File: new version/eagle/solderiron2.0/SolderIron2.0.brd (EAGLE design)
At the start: 36 x 47 mm, 36 parts, among them J1 DCJ0202, X1 22-23-2021, X2 PG203J

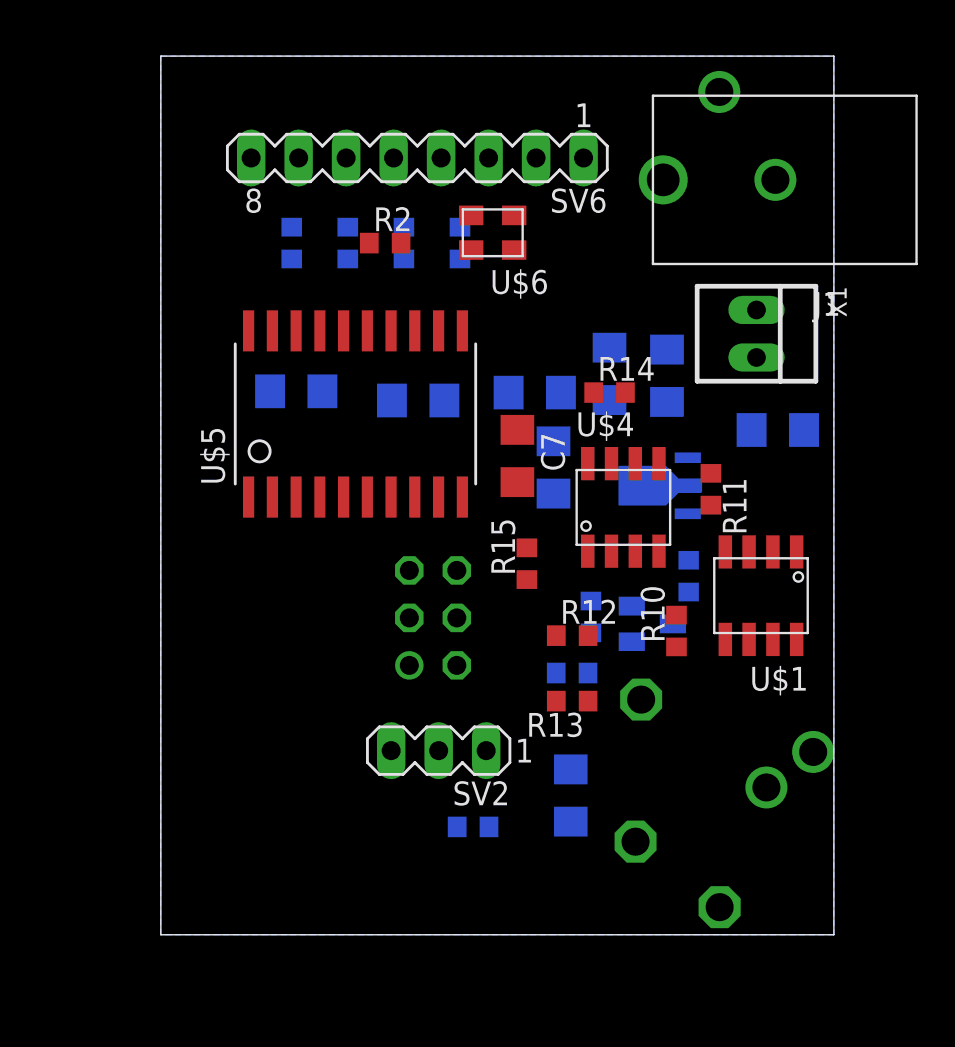
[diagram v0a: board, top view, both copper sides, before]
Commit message: routed new board
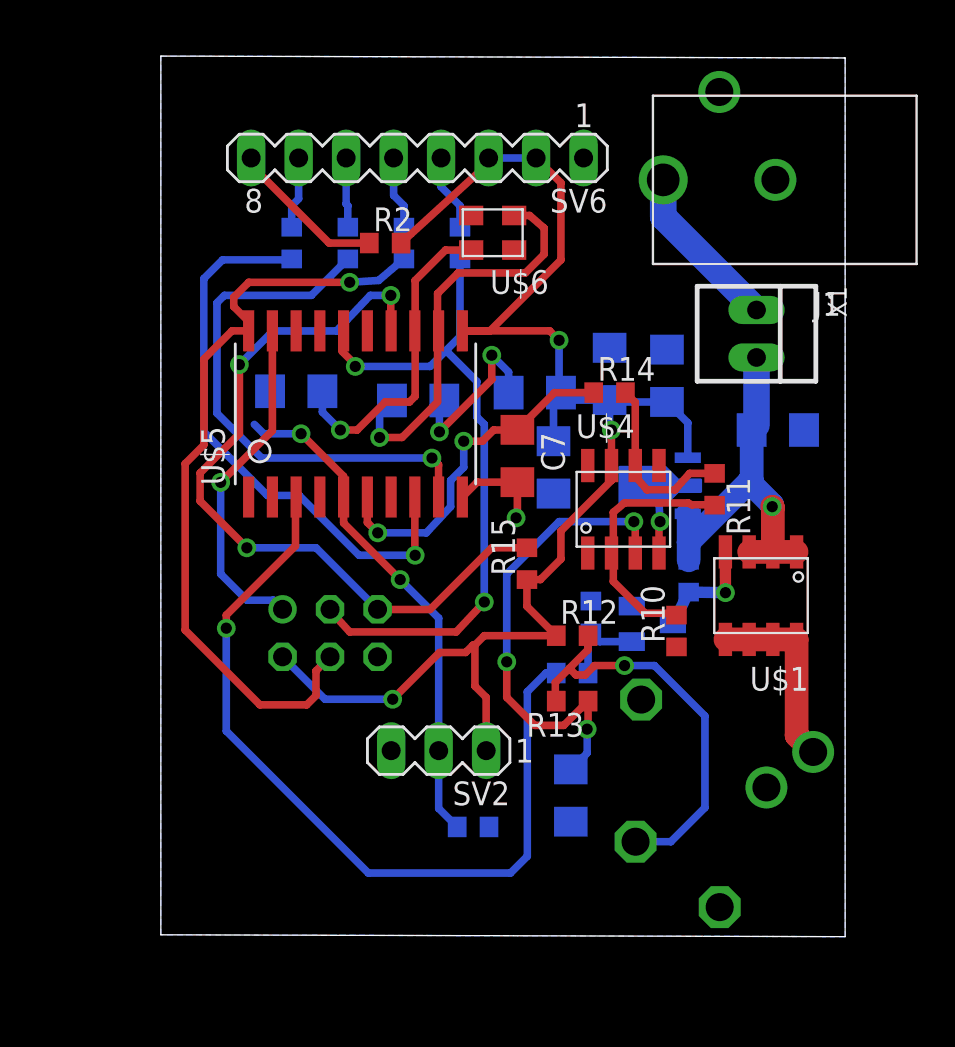
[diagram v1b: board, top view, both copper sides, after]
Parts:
- moved SV4 5.57 mm to (25.1, 34.1), turned to 180 degrees
- moved R11 0.20 mm to (45.6, 41.8)
- moved U$4 0.10 mm to (40.7, 40.8)
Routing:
- net +5V: track 0.00 -> 80.8 mm, vias 0 -> 3
- net PWM: track 0.00 -> 44.4 mm, vias 0 -> 1
- net MOSI: track 0.00 -> 41.2 mm, vias 0 -> 1
- net N$19: track 0.00 -> 41.0 mm, vias 0 -> 3
- net SCK: track 0.00 -> 36.4 mm, vias 0 -> 2
- net CS: track 0.00 -> 30.5 mm, vias 0 -> 1
- net DC: track 0.00 -> 28.6 mm, vias 0 -> 1
- net POT: track 0.00 -> 27.2 mm, vias 0 -> 2
- net N$13: track 0.00 -> 25.8 mm, vias 0 -> 3
- net SEN: track 0.00 -> 22.3 mm, vias 0 -> 1
- net N$14: track 0.00 -> 21.8 mm, vias 0 -> 1
- net V12: track 0.00 -> 20.7 mm, vias 0 -> 1
- net ADC: track 0.00 -> 18.6 mm, vias 0 -> 2
- net GND: track 0.00 -> 18.3 mm, vias 0 -> 4
- net N$15: track 0.00 -> 18.2 mm, vias 0 -> 1
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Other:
- board size 36 x 47 mm -> 36.6 x 47.1 mm

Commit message: added title to PCB
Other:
- board size 36.6 x 47.1 mm -> 37.6 x 51.1 mm
- board text added: "By: BLKBNY"
- board text added: "Solder Station V2.0"
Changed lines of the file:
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@@
 <setting verticaltext="up"/>
 </settings>
-<grid distance="0.1" unitdist="mm" unit="mm" style="lines" multiple="1" display="yes" altdistance="0.025" altunitdist="inch" altunit="inch"/>
+<grid distance="1" unitdist="mm" unit="mm" style="lines" multiple="1" display="yes" altdistance="0.025" altunitdist="inch" altunit="inch"/>
 <layers>
 <layer number="1" name="Top" color="4" fill="1" visible="yes" active="yes"/>
@@
 <board>
 <plain>
-<wire x1="16" y1="18" x2="52.6" y2="17.9" width="0" layer="20"/>
-<wire x1="52.6" y1="17.9" x2="52.6" y2="64.9" width="0" layer="20"/>
-<wire x1="52.6" y1="64.9" x2="16" y2="65" width="0" layer="20"/>
-<wire x1="16" y1="65" x2="16" y2="18" width="0" layer="20"/>
+<wire x1="16" y1="15" x2="53.6" y2="14.9" width="0" layer="20"/>
+<wire x1="53.6" y1="14.9" x2="53.6" y2="65.9" width="0" layer="20"/>
+<wire x1="53.6" y1="65.9" x2="16" y2="66" width="0" layer="20"/>
+<wire x1="16" y1="66" x2="16" y2="15" width="0" layer="20"/>
+<text x="39" y="22" size="1.778" layer="1" rot="R180">Solder Station V2.0 </text>
+<text x="31" y="19" size="1.778" layer="1" rot="R180">By: BLKBNY</text>
 </plain>
 <attributes>
@@
 <contactref element="C9" pad="2"/>
 <contactref element="C8" pad="2"/>
-<polygon width="0.4064" layer="16">
-<vertex x="16" y="65"/>
-<vertex x="52.6" y="64.9"/>
-<vertex x="52.6" y="17.9"/>
-<vertex x="16" y="18"/>
-</polygon>
 <wire x1="35.07" y1="42.21" x2="32.92" y2="42.21" width="0.4064" layer="1"/>
 <wire x1="32.92" y1="42.21" x2="32.125" y2="41.415" width="0.4064" layer="1"/>
@@
 <wire x1="35.07" y1="42.21" x2="35.07" y2="40.37" width="0.4064" layer="1"/>
 <wire x1="35.07" y1="40.37" x2="35" y2="40.3" width="0.4064" layer="1"/>
+<polygon width="0.4064" layer="16">
+<vertex x="17" y="66"/>
+<vertex x="54" y="66" curve="-90"/>
+<vertex x="55" y="65"/>
+<vertex x="55" y="15" curve="-90"/>
+<vertex x="54" y="14"/>
+<vertex x="16" y="14" curve="-90"/>
+<vertex x="15" y="15"/>
+<vertex x="15" y="65" curve="-90"/>
+<vertex x="16" y="66"/>
+</polygon>
 <wire x1="41.19" y1="35.58" x2="43.58" y2="33.4" width="0" layer="19" extent="1-16"/>
 </signal>
